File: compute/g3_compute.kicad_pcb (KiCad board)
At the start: 4 copper layers, 100 x 100 mm, 106 parts, among them IC101 CD74AC153M96, J101 Conn_01x09_Male, J102 53398-0871, J103 Temp_Connector_1x4, J104 53398-0671, J105 Conn_01x10_Male, J106 Pi_Connector, J107 Conn_01x06_Male, J108 CONSMA001-SMD-G, J109 CONSMA001-SMD-G, J110 CONSMA001-SMD-G, Q101 PBSS4140DPN, U101 LoRa-E5, U102 PA1616D, U201 SX1262, U202 PE4259, Y201 TBD

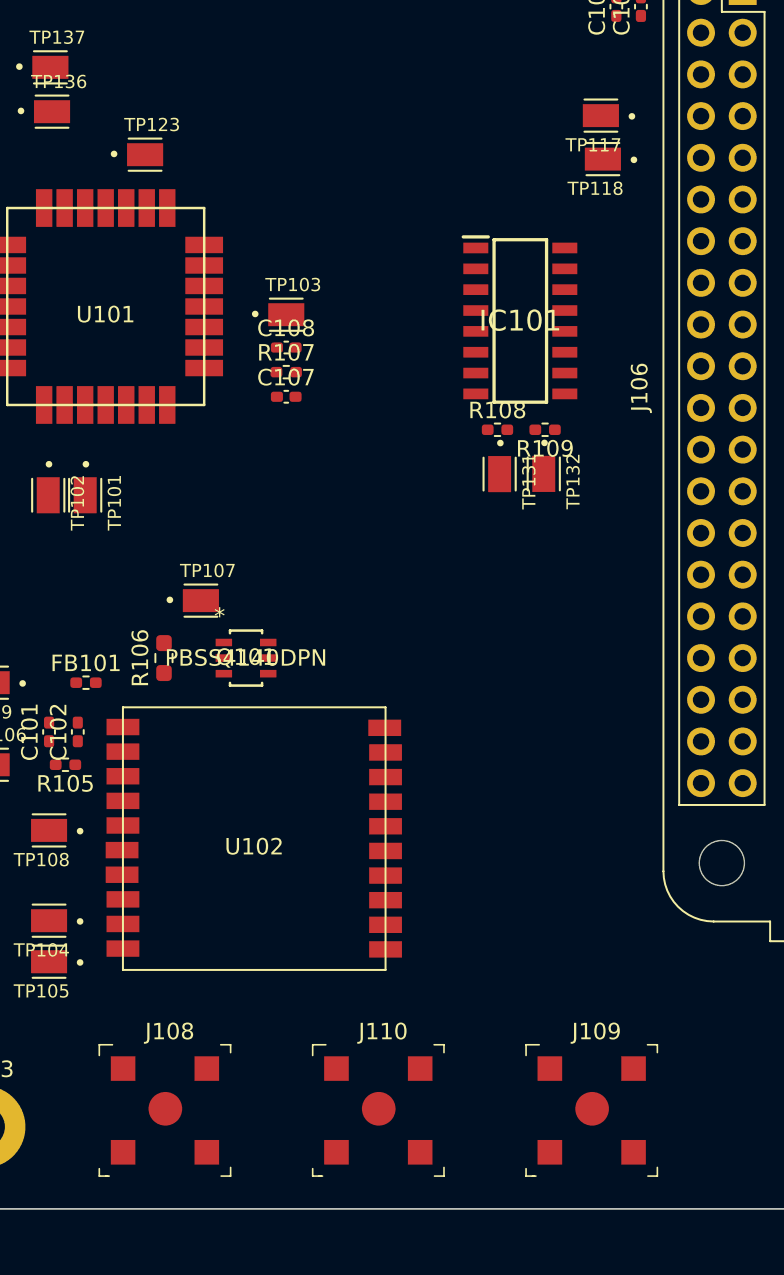
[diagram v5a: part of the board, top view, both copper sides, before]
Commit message: Changed pinnout of UART MUX to make routing easier
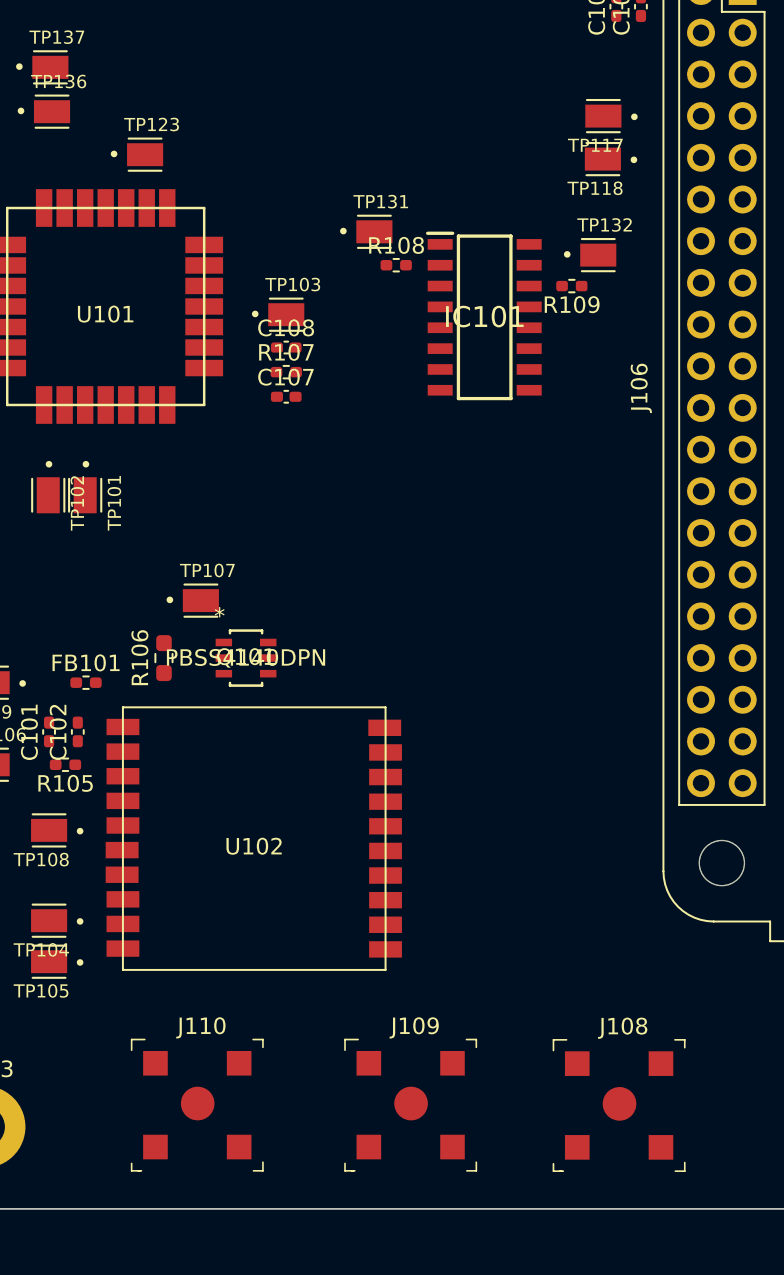
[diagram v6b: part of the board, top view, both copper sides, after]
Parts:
- moved J108 27.7 mm to (143.7, 143.7)
- moved TP131 16.6 mm to (128.8, 90.5), turned to 0 degrees
- moved TP132 13.7 mm to (142.4, 91.9), turned to 0 degrees
- moved R108 11.8 mm to (130.1, 92.5)
- moved J109 11.0 mm to (131.0, 143.7)
- moved J110 11.0 mm to (118.0, 143.7)
- moved R109 8.91 mm to (140.8, 93.8)
- moved IC101 2.18 mm to (135.5, 95.7)
- moved TP117 0.15 mm to (142.7, 83.4)
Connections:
- IC101 pad 10: /LOAD_TX -> /GPS_TX
- IC101 pad 12: /CPPC_TX -> /LOAD_TX
- IC101 pad 13: /GPS_TX -> /CPPC_TX
- IC101 pad 3: /GPS_RX -> /CPPC_RX
- IC101 pad 4: /CPPC_RX -> /LOAD_RX
- IC101 pad 6: /LOAD_RX -> /GPS_RX
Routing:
- added copper zone on 3V3, net +3V3
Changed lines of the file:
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@@
   (layers
     (0 F.Cu signal)
-    (1 GND power hide)
+    (1 GND power)
     (2 3V3 power)
     (31 B.Cu signal)
@@
     (mod_text_size 1 1)
     (mod_text_width 0.15)
-    (pad_size 2.2 1.4)
+    (pad_size 0.65 1.525)
     (pad_drill 0)
     (pad_to_mask_clearance 0)
     (aux_axis_origin 0 0)
     (grid_origin 20 20)
-    (visible_elements 7FFFFFFF)
+    (visible_elements 7FFFF7FF)
     (pcbplotparams
       (layerselection 0x010fc_ffffffff)
@@
   )
   (module Perch:HARWIN_S2751-46R (layer F.Cu)
-    (at 139.08 105.22 270)
-    (fp_text reference TP132 (at 0.44 -1.808 90) (layer F.SilkS)
+    (at 142.4 91.89)
+    (fp_text reference TP132 (at 0.44 -1.808) (layer F.SilkS)
       (effects (font (size 0.8 0.8) (thickness 0.15)))
     )
-    (fp_text value TestPoint (at 5.898 1.572 90) (layer F.Fab)
+    (fp_text value TestPoint (at 5.898 1.572) (layer F.Fab)
       (effects (font (size 0.8 0.8) (thickness 0.15)))
     )
@@
     (fp_line (start -1 -0.98) (end 1 -0.98) (layer F.SilkS) (width 0.127))
     (fp_line (start 1 0.98) (end -1 0.98) (layer F.SilkS) (width 0.127))
-    (pad 1 smd rect (at 0 0 270) (size 2.2 1.4) (layers F.Cu F.Paste F.Mask)
+    (pad 1 smd rect (at 0 0) (size 2.2 1.4) (layers F.Cu F.Paste F.Mask)
       (net 56 /MUX_SELB))
   )
   (module Perch:HARWIN_S2751-46R (layer F.Cu)
-    (at 136.39 105.23 270)
-    (fp_text reference TP131 (at 0.44 -1.808 90) (layer F.SilkS)
+    (at 128.76 90.47)
+    (fp_text reference TP131 (at 0.44 -1.808) (layer F.SilkS)
       (effects (font (size 0.8 0.8) (thickness 0.15)))
     )
-    (fp_text value TestPoint (at 5.898 1.572 90) (layer F.Fab)
+    (fp_text value TestPoint (at 5.898 1.572) (layer F.Fab)
       (effects (font (size 0.8 0.8) (thickness 0.15)))
     )
@@
     (fp_line (start -1 -0.98) (end 1 -0.98) (layer F.SilkS) (width 0.127))
     (fp_line (start 1 0.98) (end -1 0.98) (layer F.SilkS) (width 0.127))
-    (pad 1 smd rect (at 0 0 270) (size 2.2 1.4) (layers F.Cu F.Paste F.Mask)
+    (pad 1 smd rect (at 0 0) (size 2.2 1.4) (layers F.Cu F.Paste F.Mask)
       (net 47 /MUX_SELA))
   )
@@
   )
   (module Perch:HARWIN_S2751-46R (layer F.Cu)
-    (at 142.56 83.39 180)
+    (at 142.71 83.42 180)
     (fp_text reference TP117 (at 0.44 -1.808) (layer F.SilkS)
       (effects (font (size 0.8 0.8) (thickness 0.15)))
@@
   )
   (module Resistor_SMD:R_0402_1005Metric_Pad0.72x0.64mm_HandSolder (layer F.Cu)
-    (at 139.16 102.53 180)
+    (at 140.79 93.775 180)
     (descr "Resistor SMD 0402 (1005 Metric), square (rectangular) end terminal, IPC_7351 nominal with elongated pad for handsoldering. (Body size source: IPC-SM-782 page 72, https://www.pcb-3d.com/wordpress/wp-content/uploads/ipc-sm-782a_amendment_1_and_2.pdf), generated with kicad-footprint-generator")
     (tags "resistor handsolder")
@@
   )
   (module Resistor_SMD:R_0402_1005Metric_Pad0.72x0.64mm_HandSolder (layer F.Cu)
-    (at 136.26 102.53)
+    (at 130.09 92.505)
     (descr "Resistor SMD 0402 (1005 Metric), square (rectangular) end terminal, IPC_7351 nominal with elongated pad for handsoldering. (Body size source: IPC-SM-782 page 72, https://www.pcb-3d.com/wordpress/wp-content/uploads/ipc-sm-782a_amendment_1_and_2.pdf), generated with kicad-footprint-generator")
     (tags "resistor handsolder")
@@
   )
   (module digikey-footprints:RF_SMA_Receptical_Vertical_CONSMA001-SMD-G (layer F.Cu)
-    (at 129 144)
+    (at 117.97 143.68)
     (attr smd)
     (fp_text reference J110 (at 0.3 -4.8) (layer F.SilkS)
@@
   )
   (module digikey-footprints:RF_SMA_Receptical_Vertical_CONSMA001-SMD-G (layer F.Cu)
-    (at 142 144)
+    (at 130.97 143.68)
     (attr smd)
     (fp_text reference J109 (at 0.3 -4.8) (layer F.SilkS)
@@
   )
   (module digikey-footprints:RF_SMA_Receptical_Vertical_CONSMA001-SMD-G (layer F.Cu)
-    (at 116 144)
+    (at 143.67 143.7)
     (attr smd)
     (fp_text reference J108 (at 0.3 -4.8) (layer F.SilkS)
@@
   )
   (module Perch:SOIC127P600X175-16N_MUX (layer F.Cu)
-    (at 137.65 95.9)
+    (at 135.48 95.68)
     (descr "D (R-PDSO-G16)")
     (tags "Integrated Circuit")
@@
       (net 47 /MUX_SELA))
     (pad 3 smd rect (at -2.712 -1.905 90) (size 0.65 1.525) (layers F.Cu F.Paste F.Mask)
-      (net 48 /GPS_RX))
-    (pad 4 smd rect (at -2.712 -0.635 90) (size 0.65 1.525) (layers F.Cu F.Paste F.Mask)
       (net 49 /CPPC_RX))
+    (pad 4 smd rect (at -2.712 -0.635 90) (size 0.65 1.525) (layers F.Cu F.Paste F.Mask)
+      (net 50 /LOAD_RX))
     (pad 5 smd rect (at -2.712 0.635 90) (size 0.65 1.525) (layers F.Cu F.Paste F.Mask)
       (net 20 /E5_RX))
     (pad 6 smd rect (at -2.712 1.905 90) (size 0.65 1.525) (layers F.Cu F.Paste F.Mask)
-      (net 50 /LOAD_RX))
+      (net 48 /GPS_RX))
     (pad 7 smd rect (at -2.712 3.175 90) (size 0.65 1.525) (layers F.Cu F.Paste F.Mask)
       (net 51 /PI_TXD0))
@@
       (net 52 /PI_RXD0))
     (pad 10 smd rect (at 2.712 3.175 90) (size 0.65 1.525) (layers F.Cu F.Paste F.Mask)
-      (net 53 /LOAD_TX))
+      (net 55 /GPS_TX))
     (pad 11 smd rect (at 2.712 1.905 90) (size 0.65 1.525) (layers F.Cu F.Paste F.Mask)
       (net 21 /E5_TX))
     (pad 12 smd rect (at 2.712 0.635 90) (size 0.65 1.525) (layers F.Cu F.Paste F.Mask)
-      (net 54 /CPPC_TX))
+      (net 53 /LOAD_TX))
     (pad 13 smd rect (at 2.712 -0.635 90) (size 0.65 1.525) (layers F.Cu F.Paste F.Mask)
-      (net 55 /GPS_TX))
+      (net 54 /CPPC_TX))
     (pad 14 smd rect (at 2.712 -1.905 90) (size 0.65 1.525) (layers F.Cu F.Paste F.Mask)
       (net 56 /MUX_SELB))
@@
     (polygon
       (pts
-        (xy 201.975 38.75) (xy 201.9 141.9) (xy 98.425 141.725) (xy 98.35 38.75) (xy 98.5 38.575)
-        (xy 98.675 38.5) (xy 98.575 38.35)
+        (xy 201.975 38.75) (xy 201.9 141.9) (xy 200.719008 141.898003) (xy 200.64 152.52) (xy 95.31 152.89)
+        (xy 97.98 48.59) (xy 98.357168 48.591495) (xy 98.35 38.75) (xy 98.5 38.575) (xy 98.675 38.5)
+        (xy 98.575 38.35)
+      )
+    )
+  )
+  (zone (net 30) (net_name +3V3) (layer 3V3) (hatch edge 0.508)
+    (connect_pads (clearance 0.508))
+    (min_thickness 0.254)
+    (fill yes (arc_segments 32) (thermal_gap 0.508) (thermal_bridge_width 0.508))
+    (polygon
+      (pts
+        (xy 201.51 47.16) (xy 201.06 154.52) (xy 93.91 154.21) (xy 95.59 46.39)
       )
     )

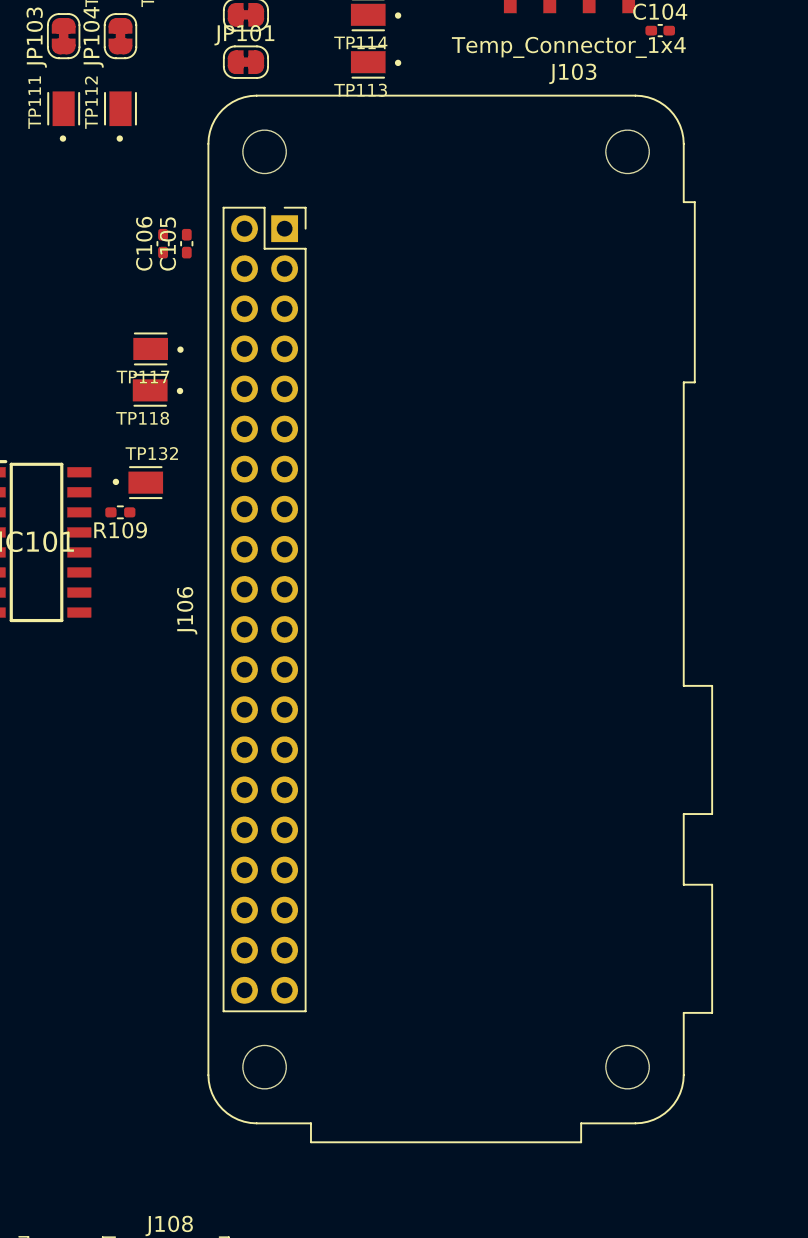
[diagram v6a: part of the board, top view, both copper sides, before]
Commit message: Changed Pi footprint
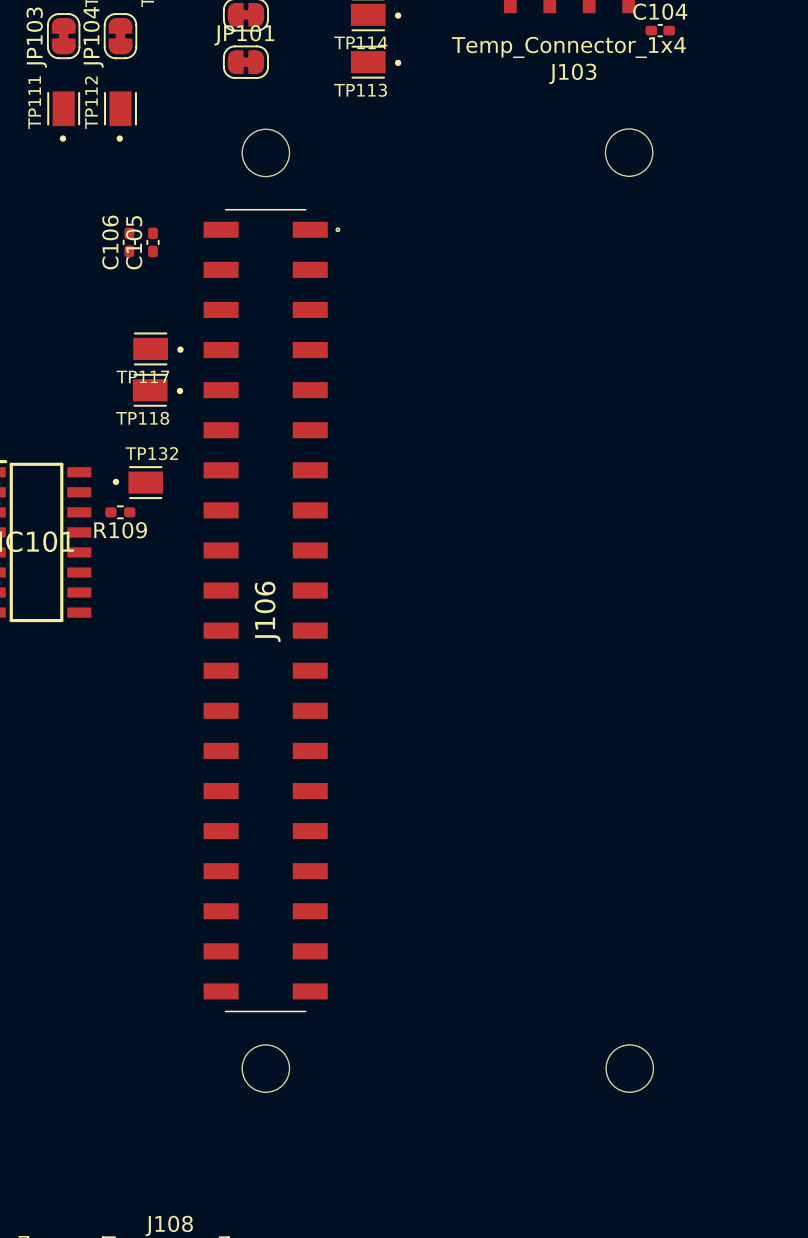
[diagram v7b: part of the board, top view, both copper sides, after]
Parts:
- J106: footprint Module:Raspberry_Pi_Zero_Socketed_THT_FaceDown_MountingHoles -> Perch:ADA3708_RaspPiZero
- moved J106 24.2 mm to (150.0, 100.0), turned to 90 degrees
- moved C105 2.14 mm to (142.9, 76.7)
- moved C106 2.14 mm to (141.4, 76.7)

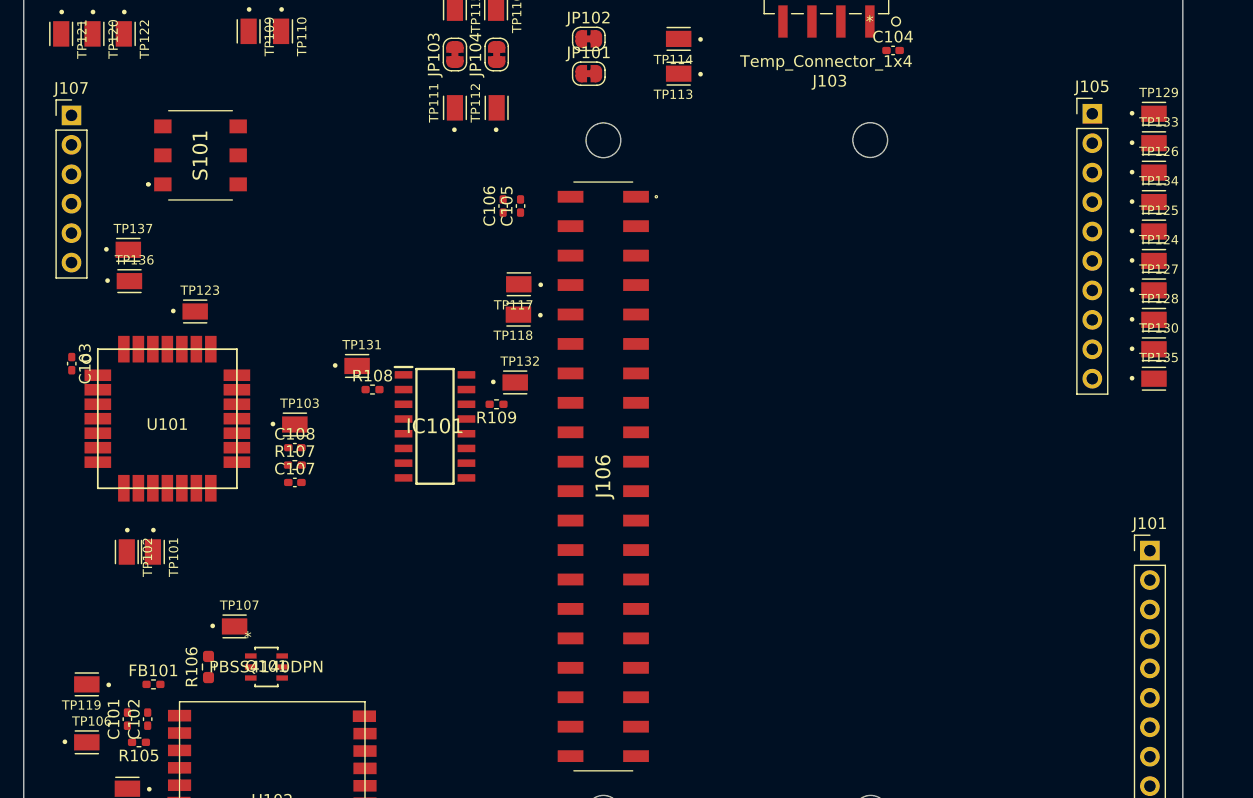
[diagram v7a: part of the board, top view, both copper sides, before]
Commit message: Routed GPIO connector to Pi
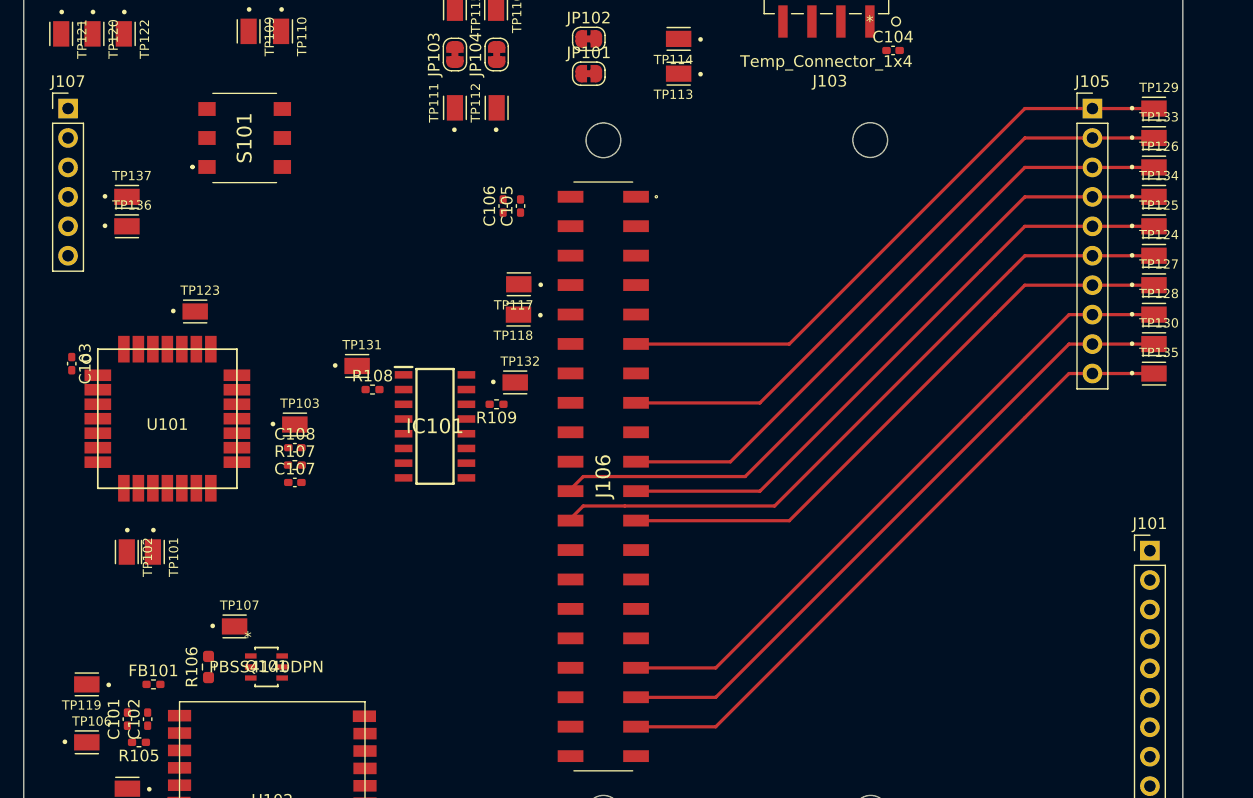
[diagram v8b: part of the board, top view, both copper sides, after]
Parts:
- moved TP136 4.74 mm to (108.9, 78.4)
- moved TP137 4.57 mm to (108.9, 75.9)
- moved S101 4.09 mm to (119.1, 70.8)
- moved J107 0.66 mm to (103.8, 68.3)
- moved J105 0.45 mm to (192.2, 68.3)
- moved TP134 0.45 mm to (197.5, 75.9)
- moved TP126 0.44 mm to (197.5, 73.3)
- moved TP124 0.44 mm to (197.5, 81.0)
- moved TP125 0.44 mm to (197.5, 78.4)
- moved TP127 0.44 mm to (197.5, 83.5)
- moved TP128 0.44 mm to (197.5, 86.0)
- moved TP129 0.44 mm to (197.5, 68.3)
- moved TP130 0.44 mm to (197.5, 88.6)
- moved TP133 0.44 mm to (197.5, 70.8)
- moved TP135 0.44 mm to (197.5, 91.1)
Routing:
- net /PI_GPIO25: track 0.00 -> 60.5 mm
- net /PI_GPIO8: track 0.00 -> 59.5 mm
- net /PI_GPIO19: track 0.00 -> 56.3 mm
- net /PI_GPIO13: track 0.00 -> 56.3 mm
- net /PI_GPIO26: track 0.00 -> 56.3 mm
- net /PI_GPIO10: track 0.00 -> 55.4 mm
- net /PI_GPIO9: track 0.00 -> 54.9 mm
- net /PI_GPIO22: track 0.00 -> 54.6 mm
- net /PI_GPIO17: track 0.00 -> 52.1 mm
- net /PI_GPIO11: track 0.00 -> 52.1 mm
